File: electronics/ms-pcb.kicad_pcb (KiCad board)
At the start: 2 copper layers, 110 x 110 mm, 27 parts, among them J1 Left motor, J2 Right motor, J3 XT60-M, U1 ESP32-S3-DEVKITC-1U-N8R2, U2 GY-521

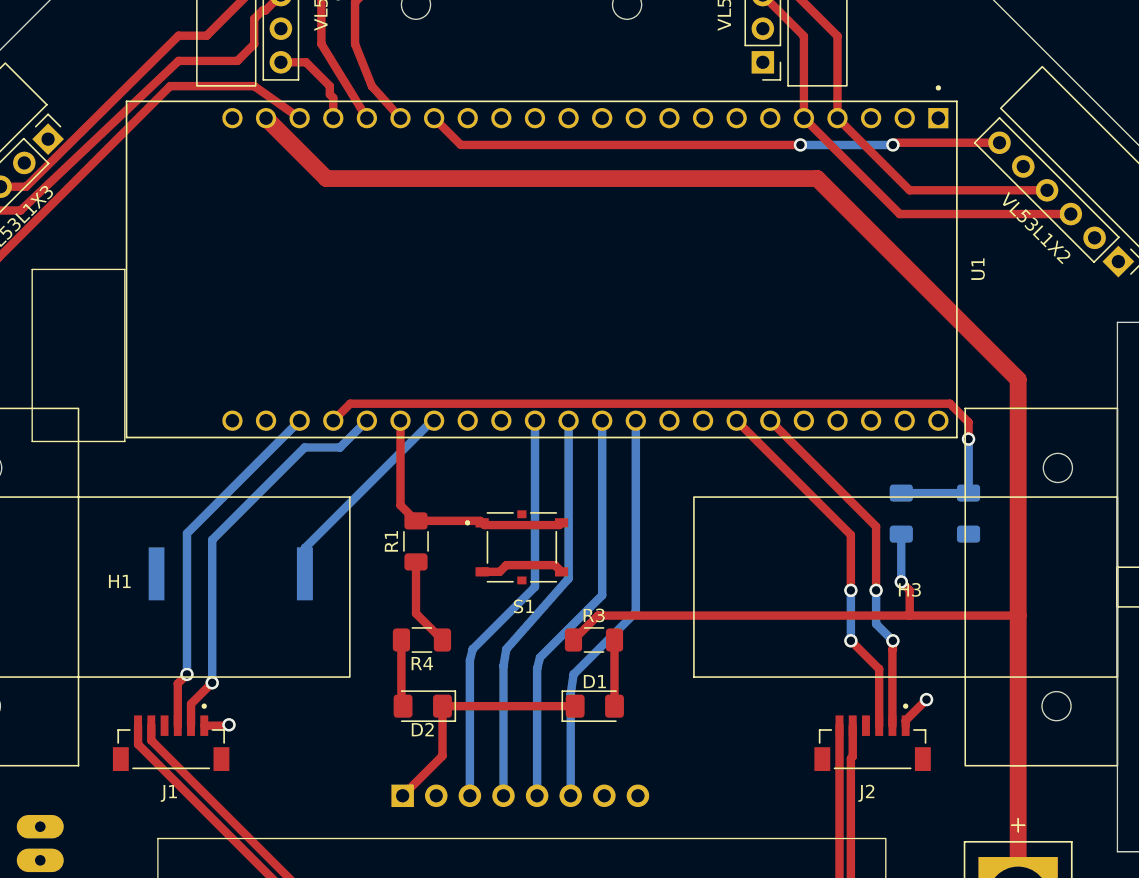
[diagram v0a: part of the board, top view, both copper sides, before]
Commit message: refactor: remove useless folder ms-pcb
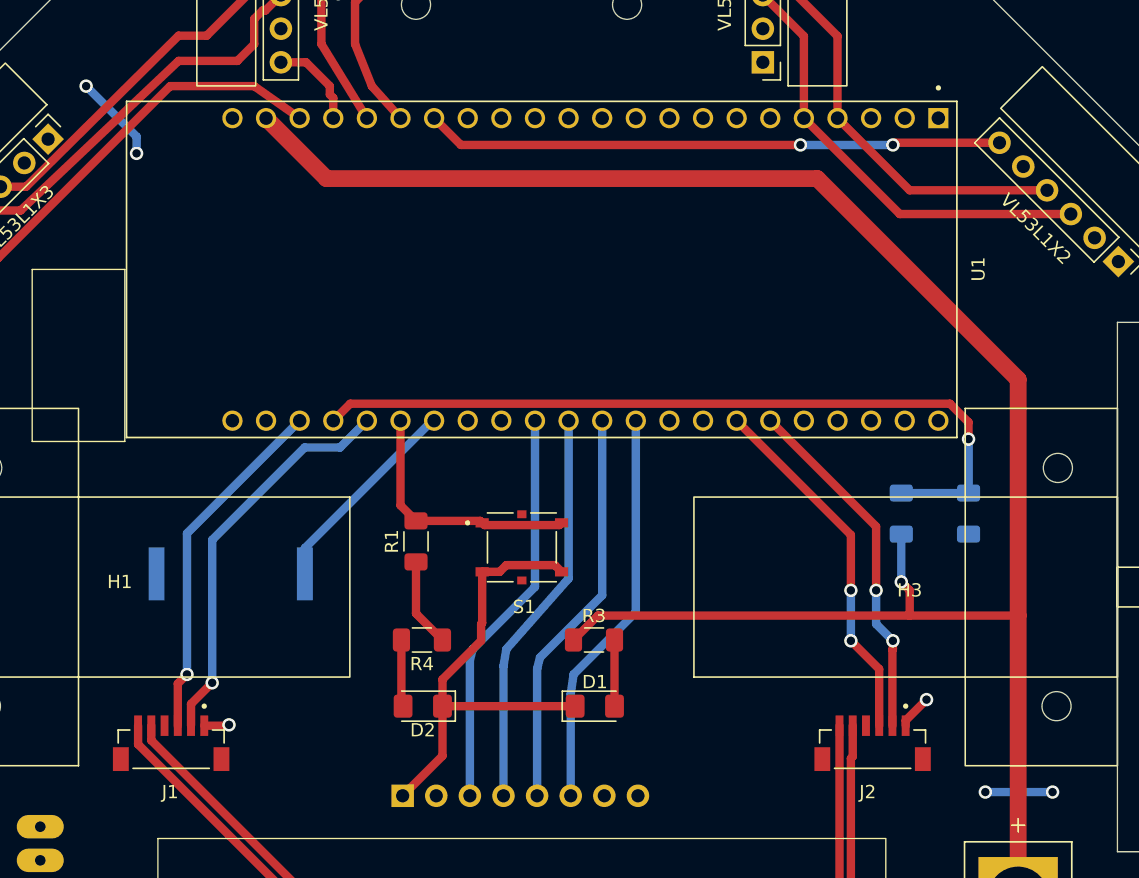
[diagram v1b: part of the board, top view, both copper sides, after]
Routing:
- net +3.3V: track 6.73 -> 18.5 mm, vias 0 -> 4
- net GND: track 29.0 -> 40.4 mm
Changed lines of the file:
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@@
 		(tags "resistor handsolder")
 		(property "Reference" "R1"
-			(at 0 -1.82 270)
+			(at 0 -1.82 -90)
 			(layer "F.SilkS")
 			(effects
@@
 		)
 		(property "Value" "20k"
-			(at 0 1.82 270)
+			(at 0 1.82 -90)
 			(layer "F.Fab")
 			(effects
@@
 		)
 		(fp_text user "${REFERENCE}"
-			(at 0 0 270)
+			(at 0 0 -90)
 			(layer "F.Fab")
 			(effects
@@
 		(tags "resistor handsolder")
 		(property "Reference" "R2"
-			(at 0 2.5 270)
+			(at 0 2.5 -90)
 			(layer "B.SilkS")
 			(effects
@@
 		)
 		(property "Value" "10k"
-			(at 0 -1.82 270)
+			(at 0 -1.82 -90)
 			(layer "B.Fab")
 			(effects
@@
 		)
 		(fp_text user "${REFERENCE}"
-			(at 0 0 270)
+			(at 0 0 -90)
 			(layer "B.Fab")
 			(effects
@@
 	)
 	(segment
+		(start 122 97.71)
+		(end 122 93.85)
+		(width 0.635)
+		(layer "F.Cu")
+		(net 1)
+	)
+	(segment
 		(start 119 104)
 		(end 119 107.762002)
@@
 	)
 	(segment
+		(start 122 93.85)
+		(end 122.05 93.85)
+		(width 0.635)
+		(layer "F.Cu")
+		(net 1)
+	)
+	(segment
 		(start 119 107.762002)
 		(end 115.991001 110.771001)
@@
 	)
 	(segment
+		(start 119 101.98)
+		(end 121.92 99.06)
+		(width 0.635)
+		(layer "F.Cu")
+		(net 1)
+	)
+	(segment
 		(start 154.000002 105.475013)
 		(end 154.000002 105.079998)
@@
 	)
 	(segment
+		(start 121.92 97.79)
+		(end 122 97.71)
+		(width 0.635)
+		(layer "F.Cu")
+		(net 1)
+	)
+	(segment
 		(start 128 93.85)
 		(end 127.495 93.345)
@@
 	(segment
 		(start 119 104)
+		(end 119 101.98)
+		(width 0.635)
+		(layer "F.Cu")
+		(net 1)
+	)
+	(segment
+		(start 119 104)
 		(end 129.025 104)
 		(width 0.635)
@@
 		(net 1)
 	)
+	(segment
+		(start 121.92 99.06)
+		(end 121.92 97.79)
+		(width 0.635)
+		(layer "F.Cu")
+		(net 1)
+	)
 	(via
 		(at 155.575 103.505)
@@
 		(net 6)
 	)
+	(via
+		(at 92.075 57.15)
+		(size 1.016)
+		(drill 0.635)
+		(layers "F.Cu" "B.Cu")
+		(free yes)
+		(net 6)
+	)
+	(via
+		(at 160.02 110.49)
+		(size 1.016)
+		(drill 0.635)
+		(layers "F.Cu" "B.Cu")
+		(free yes)
+		(net 6)
+	)
+	(via
+		(at 95.885 62.23)
+		(size 1.016)
+		(drill 0.635)
+		(layers "F.Cu" "B.Cu")
+		(free yes)
+		(net 6)
+	)
+	(via
+		(at 165.1 110.49)
+		(size 1.016)
+		(drill 0.635)
+		(layers "F.Cu" "B.Cu")
+		(free yes)
+		(net 6)
+	)
+	(segment
+		(start 95.885 60.96)
+		(end 95.885 62.23)
+		(width 0.635)
+		(layer "B.Cu")
+		(net 6)
+	)
+	(segment
+		(start 92.075 57.15)
+		(end 95.885 60.96)
+		(width 0.635)
+		(layer "B.Cu")
+		(net 6)
+	)
+	(segment
+		(start 160.02 110.49)
+		(end 165.1 110.49)
+		(width 0.635)
+		(layer "B.Cu")
+		(net 6)
+	)

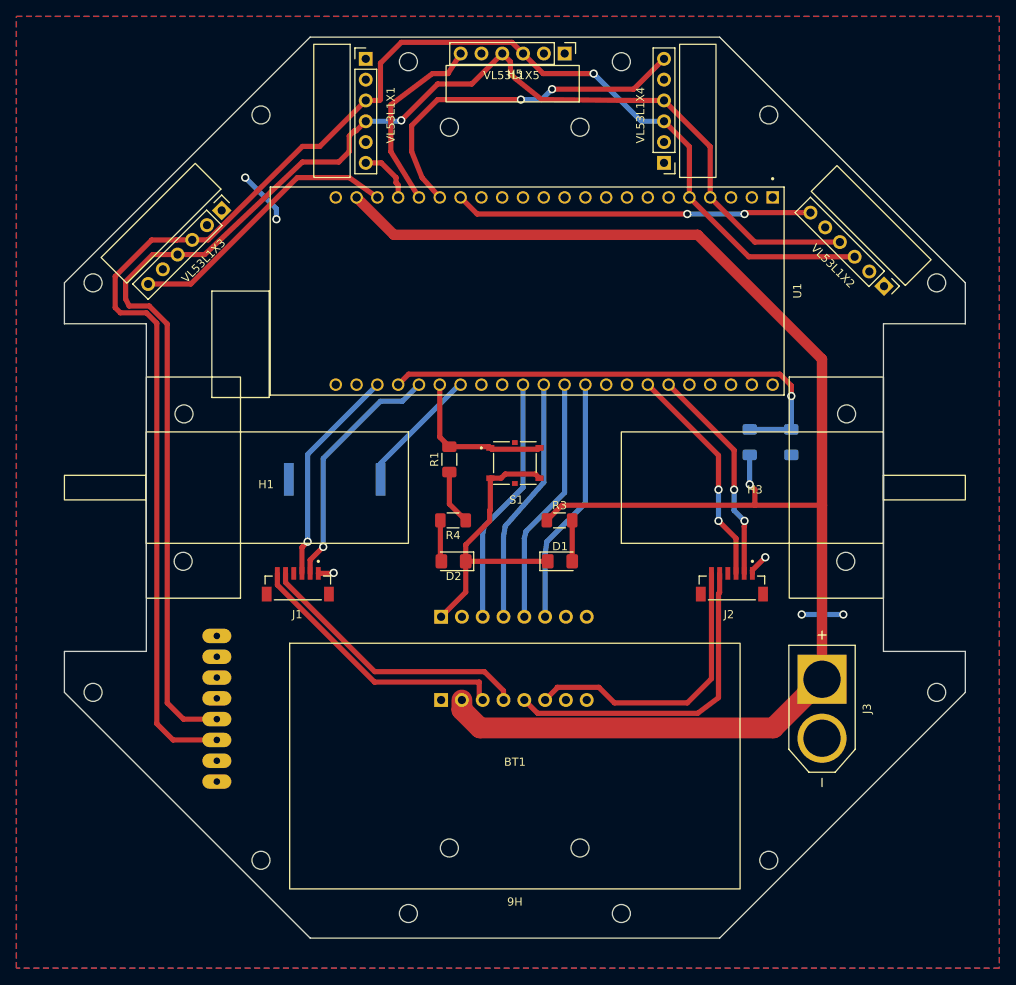
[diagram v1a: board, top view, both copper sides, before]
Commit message: elec: minor PCB layout changes
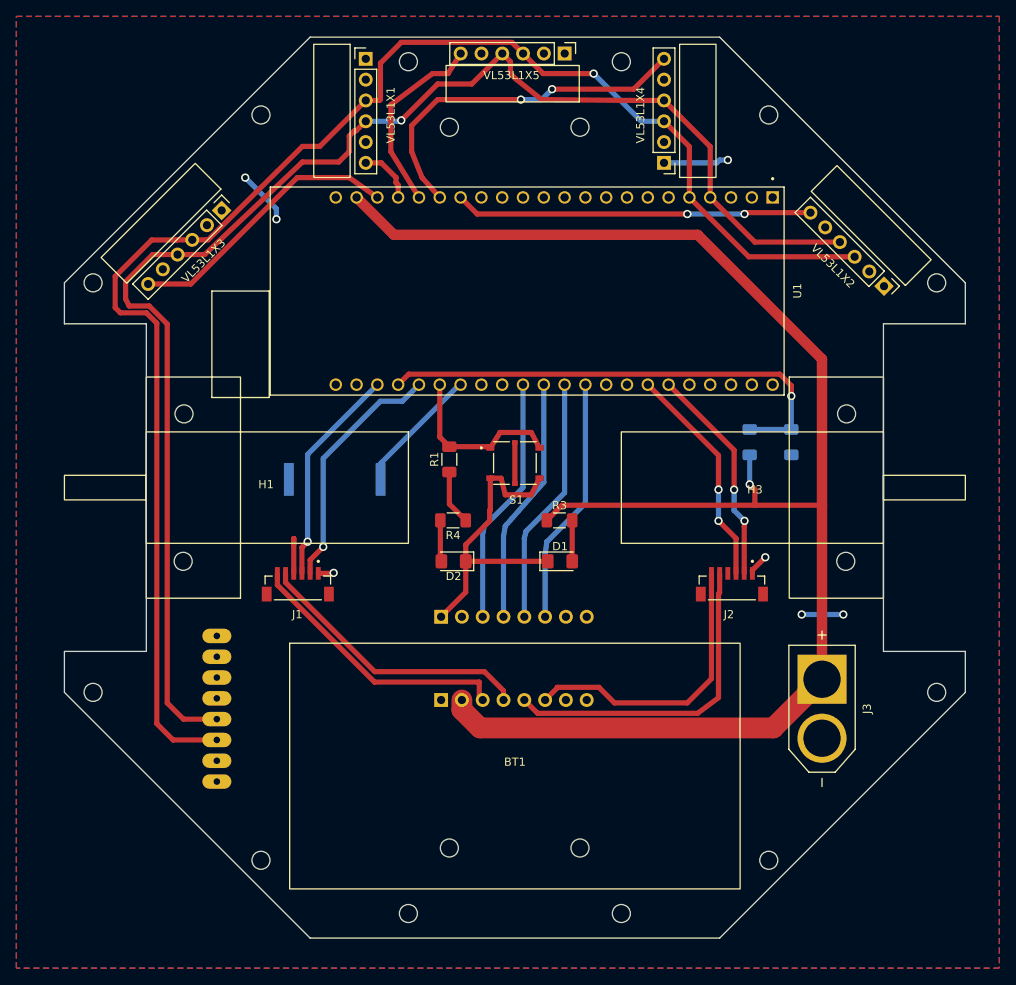
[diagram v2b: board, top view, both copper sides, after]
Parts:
- renumbered DRV1 to DRV8833
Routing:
- net +3.3V: track 18.5 -> 31.5 mm, vias 4 -> 5
- net Net-(S1-PadG1): track 0.00 -> 5.00 mm
- net GND: track 40.4 -> 42.9 mm
- net button: track 19.3 -> 21.3 mm
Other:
- board text added: "Algernon v1.0 Open-source micromouse project GitHub: @opatiny"
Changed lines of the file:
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@@
 		(at 125 40)
 		(property "Reference" "H5"
-			(at 0 4.5 0)
+			(at 0.095 -1.265 0)
 			(unlocked yes)
-			(layer "F.SilkS")
+			(layer "Cmts.User")
 			(effects
 				(font
@@
 		)
 		(fp_text user "${REFERENCE}"
-			(at 0 7.5 0)
+			(at 0.095 -1.265 0)
 			(unlocked yes)
 			(layer "F.Fab")
@@
 		(at 125 150 180)
 		(property "Reference" "H6"
-			(at 0 4.5 180)
+			(at -0.095 -1.765 0)
 			(unlocked yes)
-			(layer "F.SilkS")
+			(layer "Cmts.User")
 			(effects
 				(font
@@
 		)
 		(fp_text user "${REFERENCE}"
-			(at 0 7.5 180)
+			(at -0.095 -1.765 0)
 			(unlocked yes)
 			(layer "F.Fab")
@@
 		(tags "resistor handsolder")
 		(property "Reference" "R5"
-			(at 0 -2.5 90)
+			(at 0 -1.905 90)
 			(layer "B.SilkS")
 			(effects
@@
 		(tags "resistor handsolder")
 		(property "Reference" "R2"
-			(at 0 2.5 -90)
+			(at 0 -1.905 -90)
 			(layer "B.SilkS")
 			(effects
@@
 		(layer "B.Cu")
 		(at 125 116 -90)
-		(property "Reference" "DRV1"
+		(property "Reference" "DRV8833"
 			(at 0 11.684 90)
 			(unlocked yes)
@@
 		(layer "Edge.Cuts")
 	)
+	(gr_text "Algernon v1.0\nOpen-source micromouse project\nGitHub: @opatiny"
+		(at 134.62 67.945 0)
+		(layer "B.SilkS")
+		(effects
+			(font
+				(size 1.524 1.524)
+				(thickness 0.15)
+			)
+			(justify top mirror)
+		)
+	)
 	(segment
 		(start 122 97.71)
@@
 	)
 	(segment
-		(start 123.825 93.345)
-		(end 123.32 93.85)
-		(width 0.635)
-		(layer "F.Cu")
-		(net 1)
-	)
-	(segment
 		(start 154.000002 105.079998)
 		(end 155.575 103.505)
@@
 	)
 	(segment
-		(start 128 93.85)
-		(end 127.495 93.345)
+		(start 119 104)
+		(end 119 101.98)
 		(width 0.635)
 		(layer "F.Cu")
@@
 	)
 	(segment
-		(start 119 104)
-		(end 119 101.98)
+		(start 123.32 93.85)
+		(end 122 93.85)
 		(width 0.635)
 		(layer "F.Cu")
@@
 	)
 	(segment
-		(start 127.495 93.345)
-		(end 123.825 93.345)
+		(start 128 93.85)
+		(end 127 95.885)
 		(width 0.635)
 		(layer "F.Cu")
@@
 	)
 	(segment
-		(start 123.32 93.85)
-		(end 122 93.85)
+		(start 123.825 95.885)
+		(end 123.32 93.85)
 		(width 0.635)
 		(layer "F.Cu")
@@
 	)
 	(segment
+		(start 127 95.885)
+		(end 123.825 95.885)
+		(width 0.635)
+		(layer "F.Cu")
+		(net 1)
+	)
+	(segment
 		(start 121.92 99.06)
 		(end 121.92 97.79)
@@
 	)
 	(segment
+		(start 98 101.210006)
+		(end 98 102)
+		(width 0.635)
+		(layer "F.Cu")
+		(net 6)
+	)
+	(segment
+		(start 98.000006 105.475013)
+		(end 98.000006 101.210012)
+		(width 0.635)
+		(layer "F.Cu")
+		(net 6)
+	)
+	(segment
 		(start 117 93.1)
 		(end 117 97)
@@
 		(net 6)
 	)
+	(segment
+		(start 98.000006 101.210012)
+		(end 98 101.210006)
+		(width 0.635)
+		(layer "F.Cu")
+		(net 6)
+	)
+	(via
+		(at 151 55)
+		(size 1.016)
+		(drill 0.635)
+		(layers "F.Cu" "B.Cu")
+		(free yes)
+		(net 6)
+	)
 	(via
 		(at 92.075 57.15)
@@
 	)
 	(segment
+		(start 149.649996 55.350004)
+		(end 143.207511 55.350004)
+		(width 0.635)
+		(layer "B.Cu")
+		(net 6)
+	)
+	(segment
+		(start 150 55)
+		(end 149.649996 55.350004)
+		(width 0.635)
+		(layer "B.Cu")
+		(net 6)
+	)
+	(segment
 		(start 95.885 60.96)
 		(end 95.885 62.23)
@@
 	)
 	(segment
+		(start 151 55)
+		(end 150 55)
+		(width 0.635)
+		(layer "B.Cu")
+		(net 6)
+	)
+	(segment
 		(start 107.889993 117.475)
 		(end 97.000006 106.585013)
@@
 	)
 	(segment
-		(start 122 90.15)
-		(end 122.1675 90.3175)
+		(start 123.19 88.265)
+		(end 127 88.265)
 		(width 0.635)
 		(layer "F.Cu")
@@
 	)
 	(segment
-		(start 127.8325 90.3175)
+		(start 127 88.265)
 		(end 128 90.15)
 		(width 0.635)
@@
 	)
 	(segment
+		(start 122 90.15)
+		(end 123.19 88.265)
+		(width 0.635)
+		(layer "F.Cu")
+		(net 37)
+	)
+	(segment
 		(start 117 90)
 		(end 121.85 90)
@@
 	)
 	(segment
-		(start 122.1675 90.3175)
-		(end 127.8325 90.3175)
+		(start 125 89.5)
+		(end 125 94.5)
 		(width 0.635)
 		(layer "F.Cu")
-		(net 37)
+		(net 57)
 	)
 	(zone

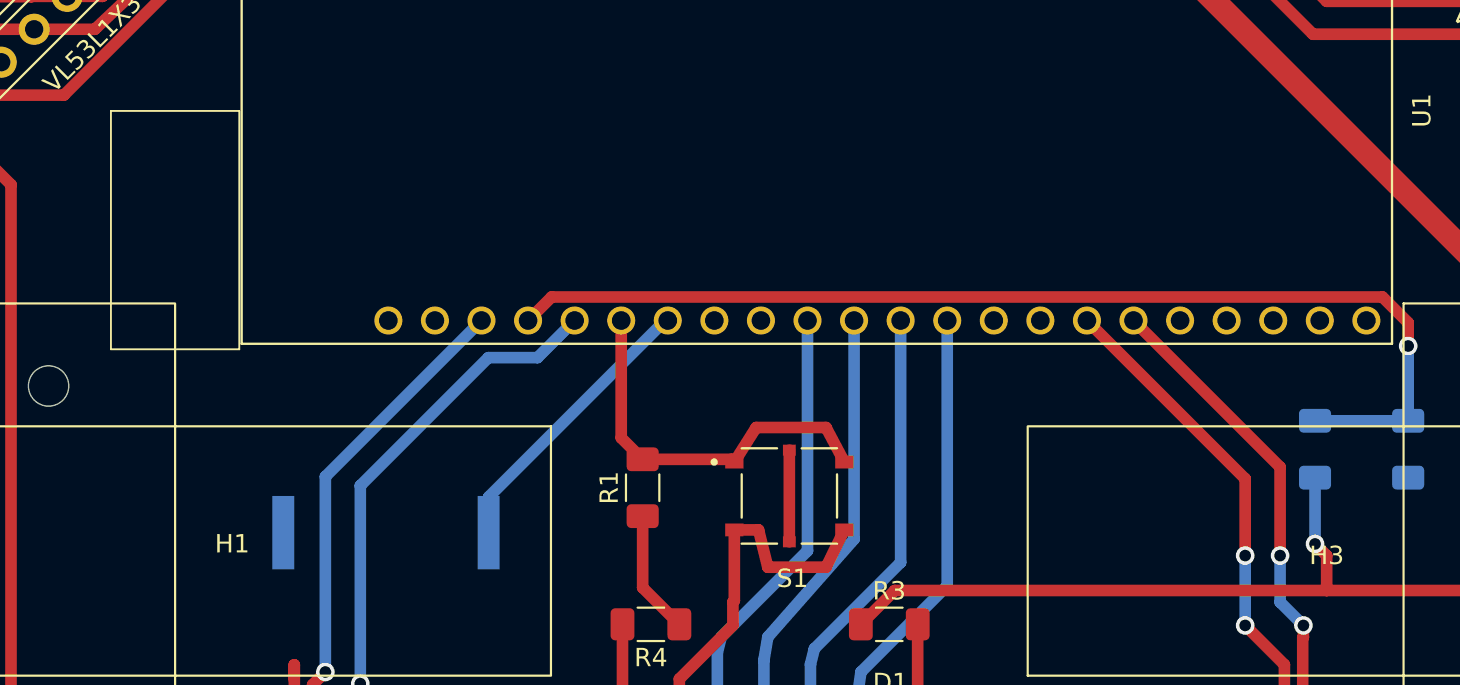
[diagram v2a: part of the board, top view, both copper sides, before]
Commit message: fix: finish PCB layout v1.0.0
Closes: #10
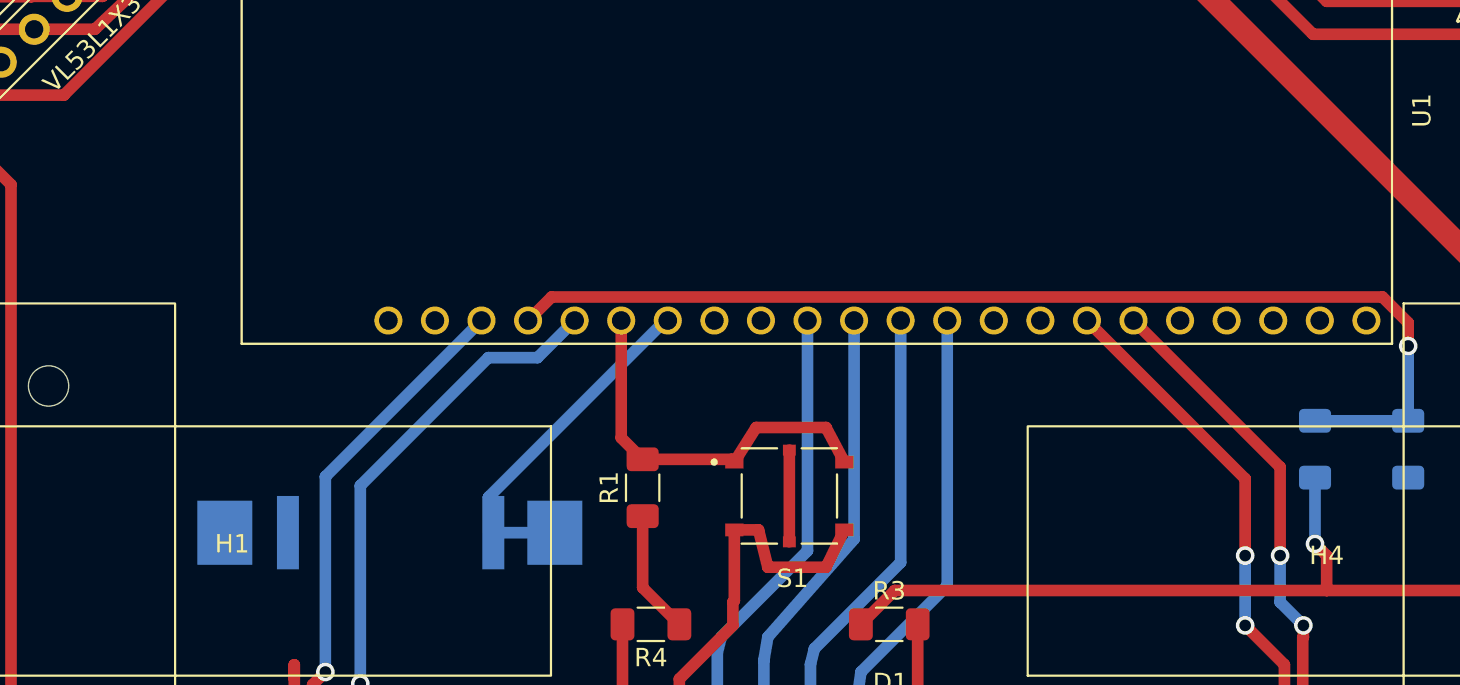
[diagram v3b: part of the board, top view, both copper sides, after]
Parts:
- added REF**: OSHW-Logo2_14.6x12mm_SilkScreen, Symbol:OSHW-Logo2_14.6x12mm_SilkScreen, B.Cu at (105.4, 71.1)
- LS1: footprint footprints:SPKR_PKLCS1212E20A0-R1 -> footprints:buzzer_double_footprint
- renumbered DRV8833 to DRV1, H5 to H3, H3 to H4, H4 to H5
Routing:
- net buzzer: track 15.7 -> 19.1 mm
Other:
- board text added: "Algernon v1.0.0 Open-source micromouse project GitHub: @opatiny"
- board text removed: "Algernon v1.0 Open-source micromouse project GitHub: @opatiny"

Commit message: elec: change debug leds resistors values
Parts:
- D1: value LED_VBAT -> GREEN
- D2: value LED_3V3 -> BLUE
- R3: value 220 -> 40k
- R4: value 220 -> 5k
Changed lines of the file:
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@@
 			)
 		)
-		(property "Value" "LED_3V3"
+		(property "Value" "BLUE"
 			(at 0 1.82 180)
 			(layer "F.Fab")
@@
 			)
 		)
-		(property "Value" "LED_VBAT"
+		(property "Value" "GREEN"
 			(at 0 1.82 0)
 			(layer "F.Fab")
@@
 			)
 		)
-		(property "Value" "220"
+		(property "Value" "5k"
 			(at 0 1.82 180)
 			(layer "F.Fab")
@@
 			)
 		)
-		(property "Value" "220"
+		(property "Value" "40k"
 			(at 0 1.82 0)
 			(layer "F.Fab")
@@
 		)
 		(property "Value" "1k"
-			(at 0 2.5 90)
+			(at 0 1.905 90)
 			(layer "B.Fab")
 			(effects
@@
 		)
 		(property "Value" "10k"
-			(at 0 -1.82 -90)
+			(at -0.085 1.905 -90)
 			(layer "B.Fab")
 			(effects
